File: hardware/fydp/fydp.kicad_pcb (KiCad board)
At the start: 2 copper layers, 104 x 64 mm, 247 parts, among them J1 1054500101, J11 Conn_01x04_Pin, J12 Conn_01x04_Pin, J14 Conn_01x02_Pin, J15 Conn_01x02_Pin, J16 Conn_01x02_Pin, J17 Conn_01x02_Pin, J18 Conn_01x02_Pin, J19 Conn_01x02_Pin, J2 Conn_01x02_Pin, J20 Conn_01x07_Pin, J3 Conn_01x02_Pin, J5 Conn_01x02_Pin, J6 Conn_01x02_Pin, J7 Conn_01x02_Pin, J8 Conn_01x08_Pin, U1 LM2733YMFX/NOPB, U10 LTC2630ISC6-LZ8-TRMPBF, U11 SN74LVC1G3157DCKR, U12 AD633ARZ-R7, U13 LTC2630ISC6-LZ8-TRMPBF, U14 SN74LVC1G3157DCKR, U15 AD633ARZ-R7, U16 LTC2630ISC6-LZ8-TRMPBF, U17 SN74LVC1G3157DCKR, U18 AD633ARZ-R7, U19 LTC2630ISC6-LZ8-TRMPBF, U2 AZ1117IH-3.3TRG1, U20 SN74LVC1G3157DCKR, U21 AD633ARZ-R7, U22 LTC2630ISC6-LZ8-TRMPBF, U23 SN74LVC1G3157DCKR, U24 AD633ARZ-R7, U25 LTC2630ISC6-LZ8-TRMPBF, U26 SN74LVC1G3157DCKR, U27 AD633ARZ-R7, U28 LTC2630ISC6-LZ8-TRMPBF, U29 SN74LVC1G3157DCKR, U3 LM2611BMF/NOPB, U30 AD633ARZ-R7, U31 LTC2630ISC6-LZ8-TRMPBF, U32 SN74LVC1G3157DCKR, U33 AD633ARZ-R7, U34 LTC2353ILX-16-PBF, U4 74HC139N, U5 74HC154D, U6 LTC2630ISC6-LZ8-TRMPBF, U7 LTC2630ISC6-LZ8-TRMPBF, U8 LTC2630ISC6-LZ8-TRMPBF, U9 LTC2630ISC6-LZ8-TRMPBF

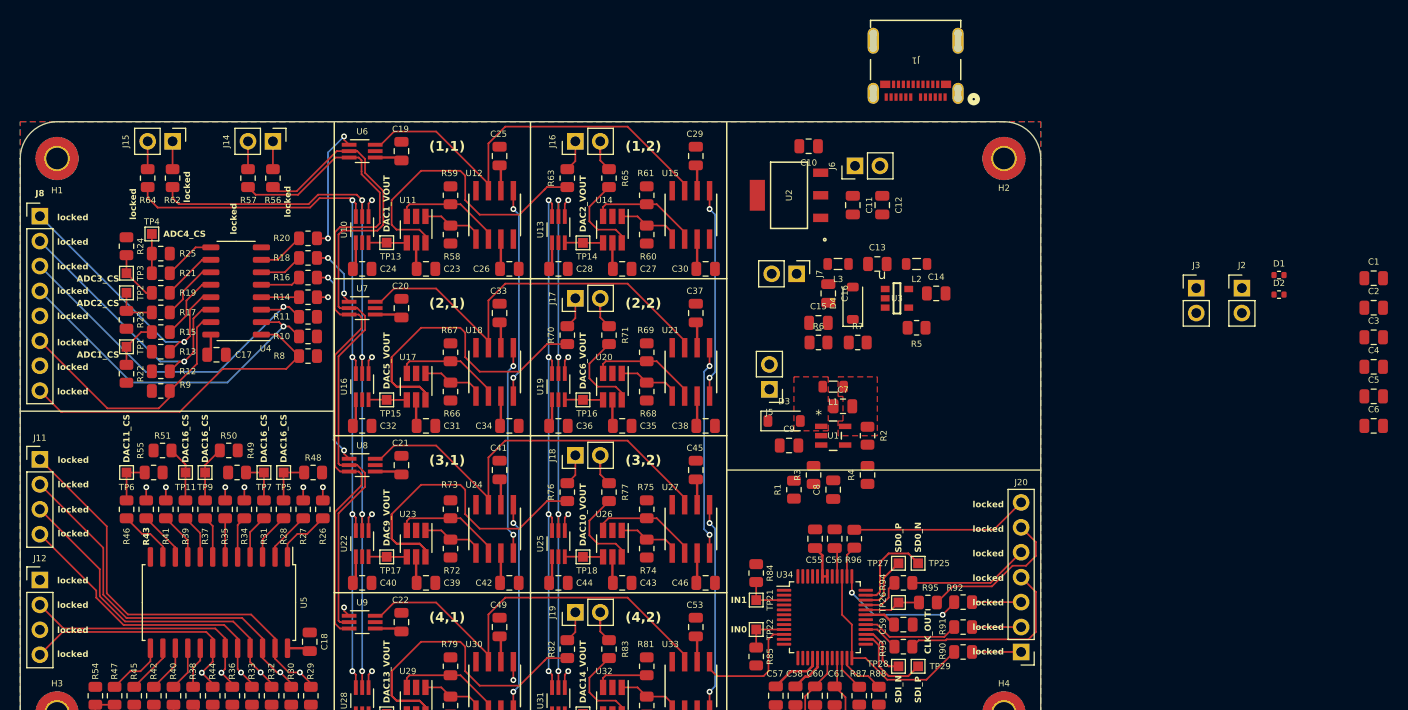
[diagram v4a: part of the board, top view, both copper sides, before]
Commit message: Initial layout is pretty much complete, need to add power planes
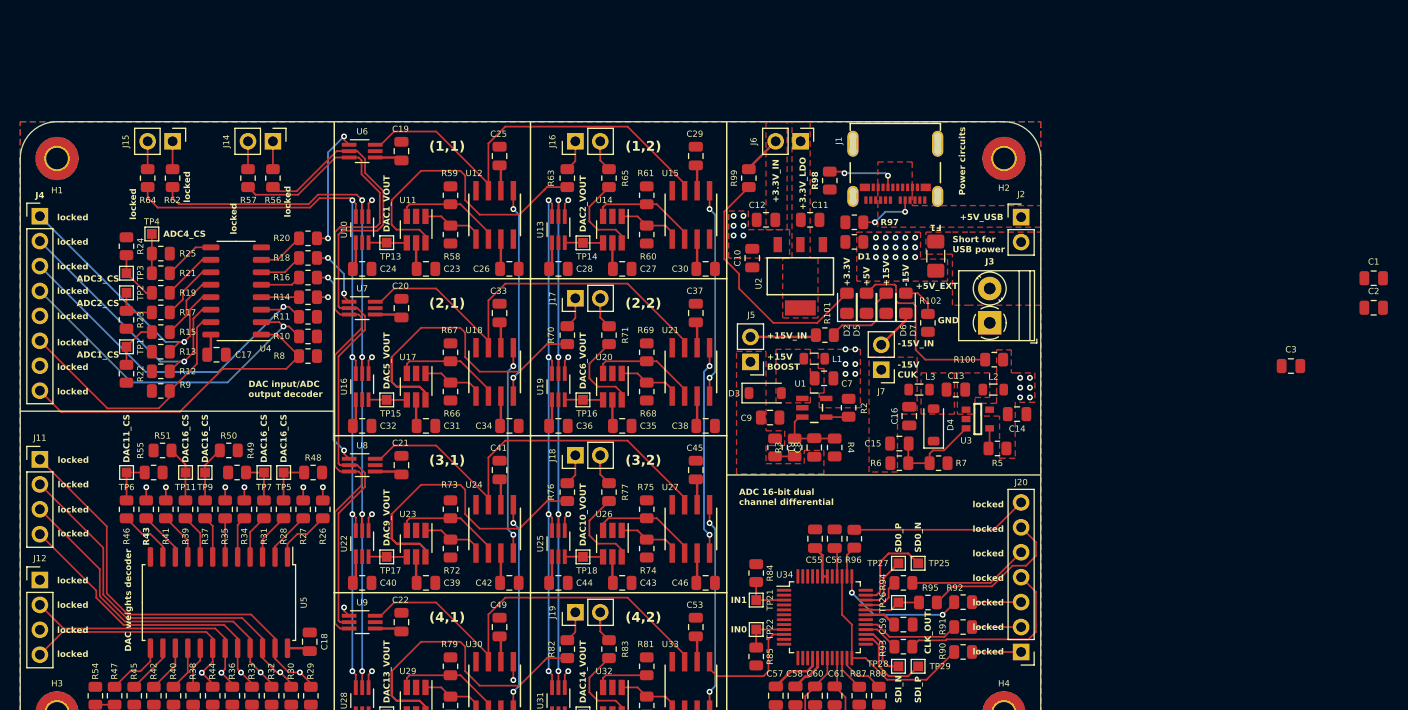
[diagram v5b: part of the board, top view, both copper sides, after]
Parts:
- removed C4, C5, C6: 4.7uF, Capacitor_SMD:C_0805_2012Metric
- removed J8: Conn_01x08_Pin, Connector_PinHeader_2.54mm:PinHeader_1x08_P2.54mm_Vertical
- added D5: LED, LED_SMD:LED_0805_2012Metric_Pad1.15x1.40mm_HandSolder, F.Cu at (195.8, 87.5)
- added D6: LED, LED_SMD:LED_0805_2012Metric_Pad1.15x1.40mm_HandSolder, F.Cu at (197.8, 87.5)
- added D7: LED, LED_SMD:LED_0805_2012Metric_Pad1.15x1.40mm_HandSolder, F.Cu at (199.8, 87.5)
- added F1: 500mA, Fuse:Fuse_1206_3216Metric_Pad1.42x1.75mm_HandSolder, F.Cu at (202.8, 82.7)
- added J4: Conn_01x08_Pin, Connector_PinHeader_2.54mm:PinHeader_1x08_P2.54mm_Vertical, F.Cu at (111.5, 78.6)
- added R100: 290, Resistor_SMD:R_0805_2012Metric, F.Cu at (208.8, 93.2)
- added R101: 1.3k, Resistor_SMD:R_0805_2012Metric, F.Cu at (191.5, 90.8)
- added R102: 1.3k, Resistor_SMD:R_0805_2012Metric, F.Cu at (202.0, 89.5)
- added R97: 5.1k, Resistor_SMD:R_0805_2012Metric, F.Cu at (194.5, 79.2)
- added R98: 5.1k, Resistor_SMD:R_0805_2012Metric, F.Cu at (192.0, 75.0)
- added R99: 120, Resistor_SMD:R_0805_2012Metric, F.Cu at (183.8, 74.8)
- D1: footprint Resistor_SMD:R_0402_1005Metric -> Resistor_SMD:R_0805_2012Metric
- D2: value TPD1E10B06DPYR -> LED; footprint Resistor_SMD:R_0402_1005Metric -> LED_SMD:LED_0805_2012Metric_Pad1.15x1.40mm_HandSolder
- J3: footprint Connector_PinHeader_2.54mm:PinHeader_1x02_P2.54mm_Vertical -> TerminalBlock_Phoenix:TerminalBlock_Phoenix_PT-1,5-2-3.5-H_1x02_P3.50mm_Horizontal
- moved D2 44.0 mm to (193.8, 87.5), turned to 90 degrees
- moved D1 43.4 mm to (194.5, 81.2), turned to 180 degrees
- moved J2 23.6 mm to (211.5, 78.7)
- moved J3 21.3 mm to (208.3, 89.5), turned to 90 degrees
- moved L3 15.2 mm to (201.1, 96.3)
- moved C13 15.1 mm to (204.8, 96.3)
- moved L2 15.0 mm to (208.7, 96.3)
- moved C16 15.0 mm to (200.1, 99.0)
- moved D4 14.9 mm to (202.6, 99.9)
- moved C14 14.8 mm to (211.1, 98.8)
- moved C15 14.8 mm to (199.1, 101.8)
- moved R5 14.8 mm to (209.1, 102.3)
- moved R6 14.8 mm to (199.1, 103.8)
- moved R7 14.8 mm to (203.1, 103.8)
- moved U3 14.8 mm to (207.1, 99.3)
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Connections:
- D2 pad 1: +5V -> GND
- D2 pad 2: GND -> Net-(D2-A)
- J1 pad A5: unconnected-(J1-PadA5) -> Net-(J1-PadA5)
- J1 pad B5: unconnected-(J1-PadB5) -> Net-(J1-PadB5)
- J2 pad 2: +5V -> /USBC RECEPTACLE/LMAO
- J3 pad 1: /USBC RECEPTACLE/PP5V0_BARREL -> GND
- J3 pad 2: +5V -> /USBC RECEPTACLE/LMAO
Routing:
- net Net-(D2-A): track 0.00 -> 25.7 mm
- net Net-(D5-A): track 0.00 -> 19.5 mm
- net /POWER/CUK1_FB: track 0.00 -> 9.94 mm
- net Net-(D6-A): track 0.00 -> 8.24 mm
- net Net-(J1-PadB5): track 0.00 -> 7.29 mm, vias 0 -> 2
- net /POWER/BOOST1_FB: track 0.00 -> 6.79 mm
- net +15V: track 26.6 -> 33.3 mm
- net Net-(J1-PadA5): track 0.00 -> 5.90 mm, vias 0 -> 2
- net -15V: track 28.6 -> 32.8 mm
- net +3.3V: track 7.90 -> 11.9 mm
- net Net-(D7-A): track 0.00 -> 3.76 mm
- net /POWER/BOOST1_SHDN: track 0.00 -> 2.30 mm
- net /POWER/CUK1_SHDN: track 0.00 -> 2.10 mm
- net /POWER/BOOST1_FB_R: track 0.00 -> 2.00 mm
- net +5V: vias 0 -> 33
- added copper zone on F.Cu, net +3.3V
- added copper zone on F.Cu, net /POWER/CUK1_LX
- added copper zone on F.Cu, net /POWER/CUK1_LX_C
- added copper zone on F.Cu, net /POWER/PN15V0_CUK
- added copper zone on F.Cu, net /POWER/PP15V0_BOOST
- added copper zone on F.Cu, net /POWER/PP3V3_LDO
- added copper zone on F.Cu, net /USBC RECEPTACLE/LMAO
- added copper zone on F.Cu, net /USBC RECEPTACLE/PP5V0_USBC
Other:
- board text added: "+15V"
- board text added: "+15V BOOST"
- board text added: "+15V_IN"
- board text added: "+3.3V"
- board text added: "+3.3V_IN"
- board text added: "+3.3V_LDO"
- board text added: "+5V"
- board text added: "+5V_EXT"
- board text added: "+5V_USB"
- board text added: "-15V"
- board text added: "-15V CUK"
- board text added: "-15V_IN"
- board text added: "ADC 16-bit dual channel differential"
- board text added: "DAC input/ADC output decoder"
- board text added: "DAC weights decoder"
- board text added: "GND"
- board text added: "Power circuits"
- board text added: "Schematic by Max Zhou Layout by Mingze Jin"
- board text added: "Short for USB power"
